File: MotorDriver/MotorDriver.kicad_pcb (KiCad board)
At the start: 2 copper layers, 70 x 70 mm, 95 parts, among them J1 Conn_01x01, J2 Conn_01x01, J3 Conn_01x01, J4 Conn_01x01, J5 Conn_02x05_Odd_Even, J6 Conn_02x03_Odd_Even, J7 4P4C, J8 4P4C, Q1 Q_NMOS_GDS, Q2 Q_NMOS_GDS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

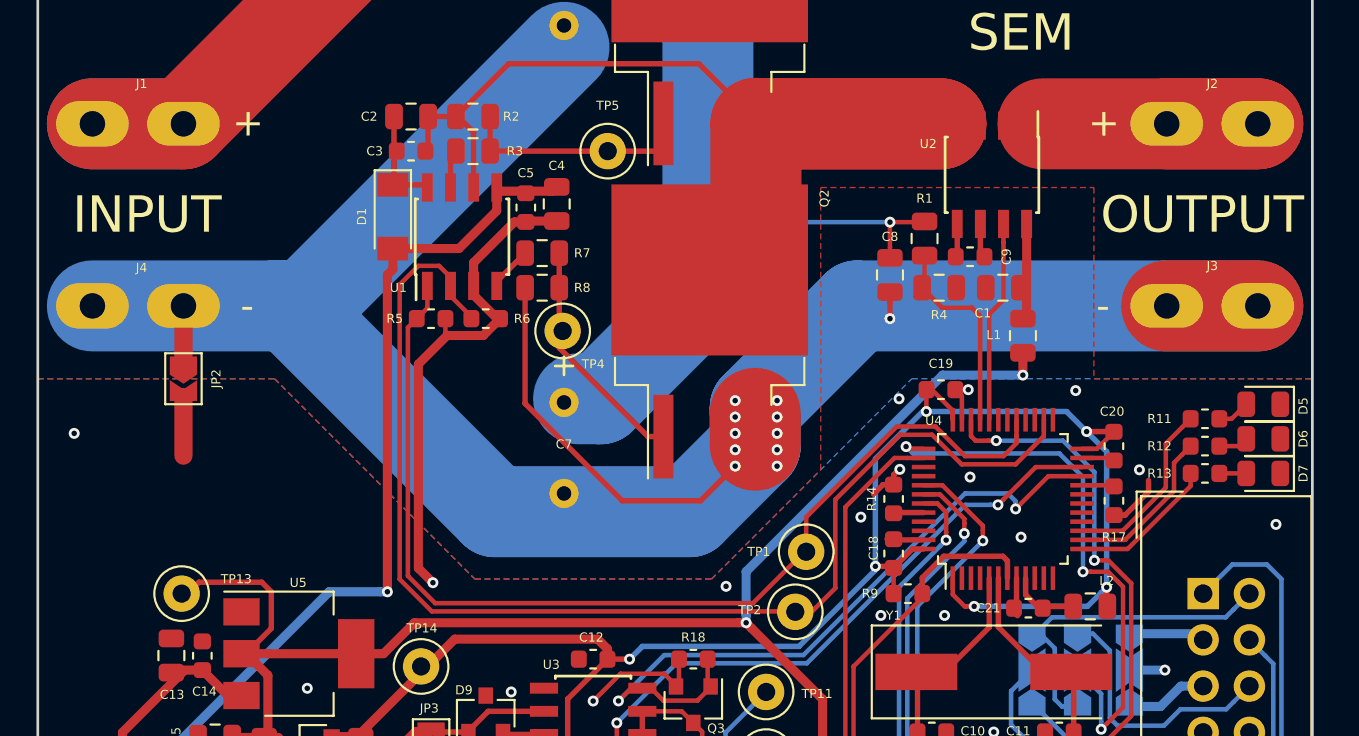
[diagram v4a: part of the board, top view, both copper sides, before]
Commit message: Added 3D models to the library
Squashed commit of the following:

commit 8070c09fc3d8f70a7cb84d0f12b6782c2c87c14c
Author: Paweł <mackipawel@gmail.com>
Date:   Mon May 6 20:26:56 2019 +0200

    Added SystemSupply 3d models.

commit 94ef8708632c7bc91211bc6ded4e0c8fb9ccef4a
Author: Paweł <mackipawel@gmail.com>
Date:   Mon May 6 01:08:52 2019 +0200

    Added 3D models to SystemSupply.

commit eb394d70be979be958e4acab21accb1817e8e0e5
Author: Paweł <mackipawel@gmail.com>
Date:   Mon May 6 00:55:39 2019 +0200

    Added 3D model to MotorController.

commit fd89e01e0ef36f85afad3e8686d3deffdf36454d
Author: Paweł <mackipawel@gmail.com>
Date:   Mon May 6 00:40:56 2019 +0200

    Added 3D models in MotorDriver.

commit 899d106fa8d45578189a4955328047d8f9558beb
Author: Paweł <mackipawel@gmail.com>
Date:   Mon May 6 00:09:40 2019 +0200

    Added 3D models to SafetySupply.

commit 06c807994bb47431d2802a96796741a0e8fb9ae5
Author: Paweł <mackipawel@gmail.com>
Date:   Sun May 5 23:17:48 2019 +0200

    Added 3D models to SafetySystem.
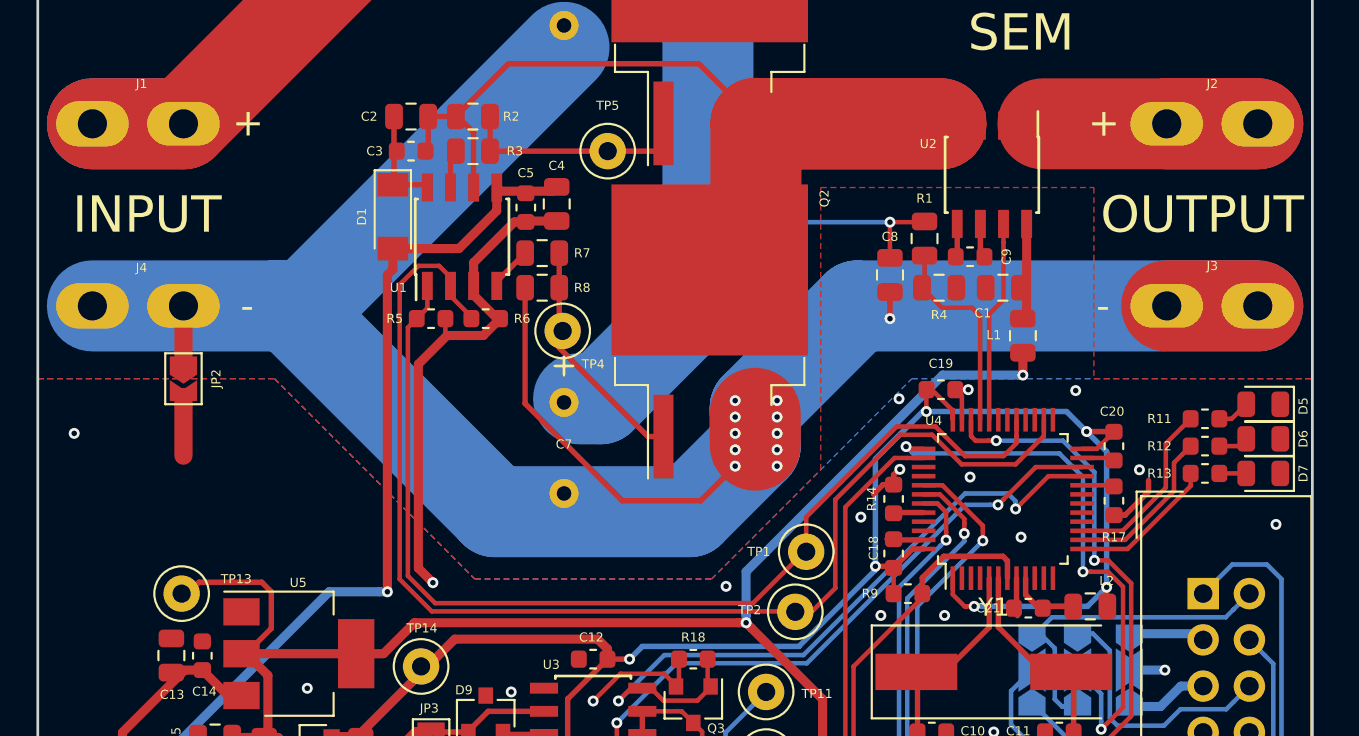
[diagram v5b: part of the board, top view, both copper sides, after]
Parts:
- Y1: footprint Crystal:Crystal_SMD_HC49-SD -> Footprints:Crystal_SMD_HC49-SD

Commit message: Adding gerbers
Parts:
- renumbered G1 to ?

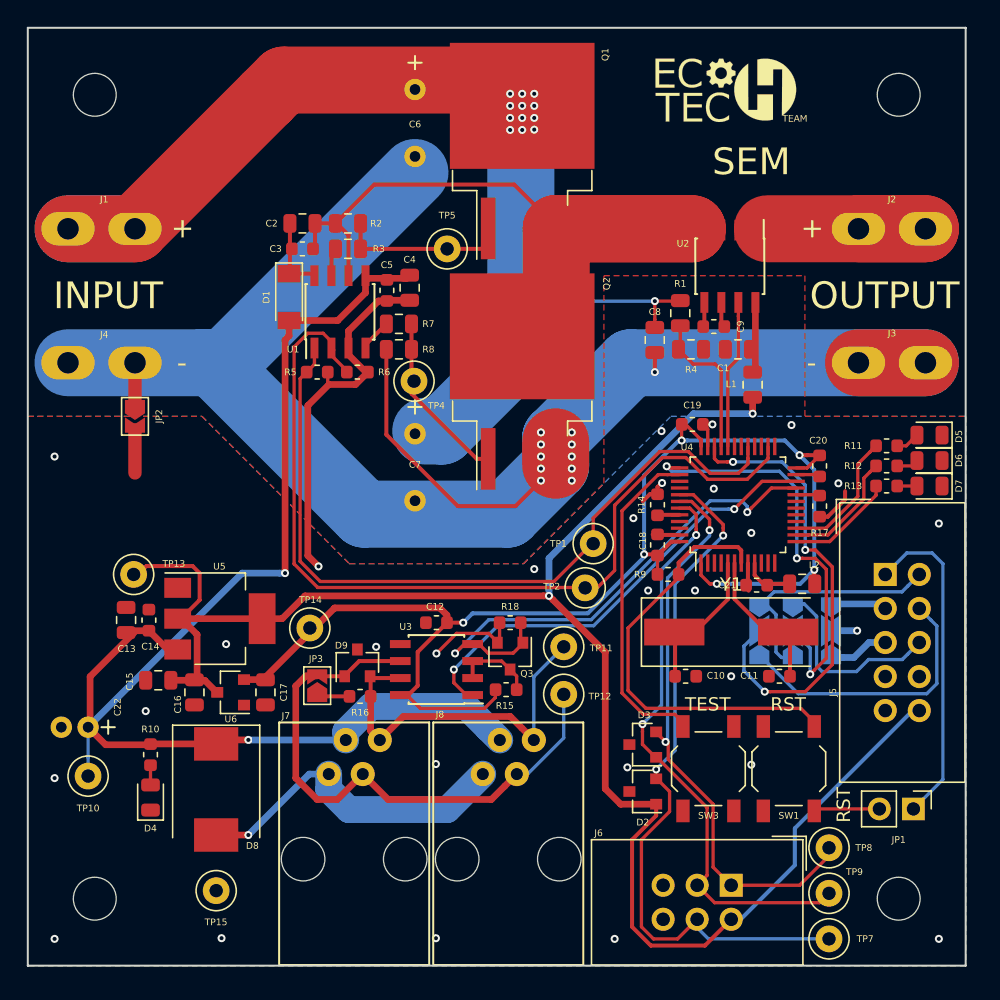
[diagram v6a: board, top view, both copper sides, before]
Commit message: Changed all via diameters to 0.7. Added project and version label on silk screen. Added more grounding vias.
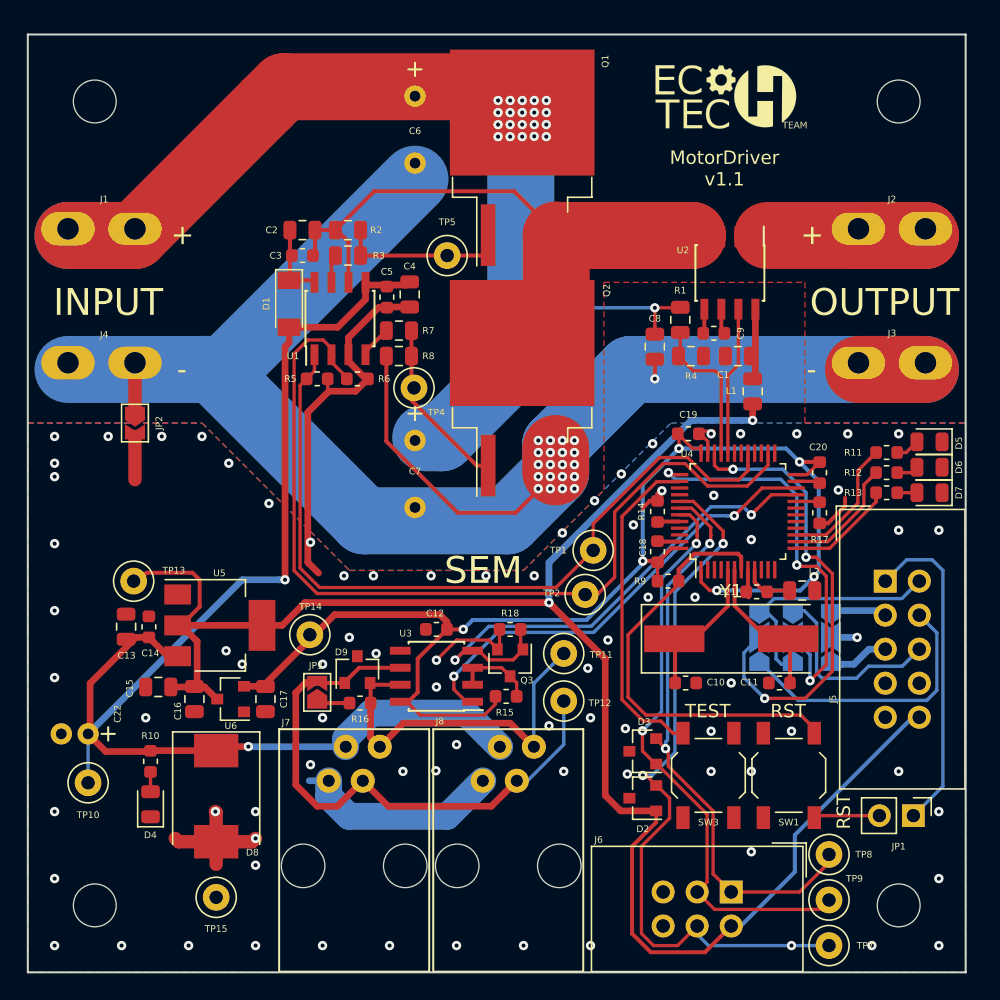
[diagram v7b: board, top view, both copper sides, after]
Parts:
- moved C19 0.76 mm to (149.3, 100.3)
- moved ? 0.50 mm to (152.2, 75.4)
- moved C1 0.50 mm to (153.0, 94.5)
- moved C10 0.50 mm to (149.1, 118.9)
- moved C11 0.50 mm to (156.1, 118.9)
- moved C12 0.50 mm to (130.5, 114.9)
- moved C13 0.50 mm to (107.3, 114.7)
- moved C14 0.50 mm to (109.0, 114.7)
- moved C15 0.50 mm to (109.7, 119.2)
- moved C16 0.50 mm to (112.4, 120.1)
- moved C17 0.50 mm to (117.7, 120.1)
- moved C18 0.50 mm to (147.0, 109.1)
- moved C2 0.50 mm to (120.5, 85.1)
- moved C20 0.50 mm to (159.1, 103.2)
- moved C21 0.50 mm to (154.4, 112.1)
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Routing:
- net GND: track 81.2 -> 83.0 mm, vias 30 -> 82
- net /ENCI: track 53.4 -> 54.8 mm, vias 2 -> 3
- net Net-(C6-Pad2): vias 11 -> 21
- net Net-(C6-Pad1): vias 13 -> 21
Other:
- net class Default: trace_width 0.25 -> 0.2; via_dia 0.6 -> 0.7
- rule trace_min: 0.24 -> 0.2
- rule via_min_size: 0.4 -> 0.7
- board text added: "MotorDriver v1.1"

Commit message: Changed 1.1 to 1.0 versions.
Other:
- board text added: "MotorDriver v1.0"
- board text removed: "MotorDriver v1.1"
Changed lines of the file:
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@@
     )
   )
-  (gr_text "MotorDriver\nv1.1" (at 152 80.5) (layer F.SilkS)
+  (gr_text "MotorDriver\nv1.0" (at 152 80.5) (layer F.SilkS)
     (effects (font (size 1 1) (thickness 0.2)))
   )
